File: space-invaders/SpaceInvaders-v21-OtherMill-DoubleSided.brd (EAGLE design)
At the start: 91.4 x 91.4 mm, 26 parts, among them J2-J4 TM4C123GXL, J3-J1 TM4C123GXL, J5 NOKIA_5110, J6 NOKIA_5110, J7 9V, U1 LM7805CT

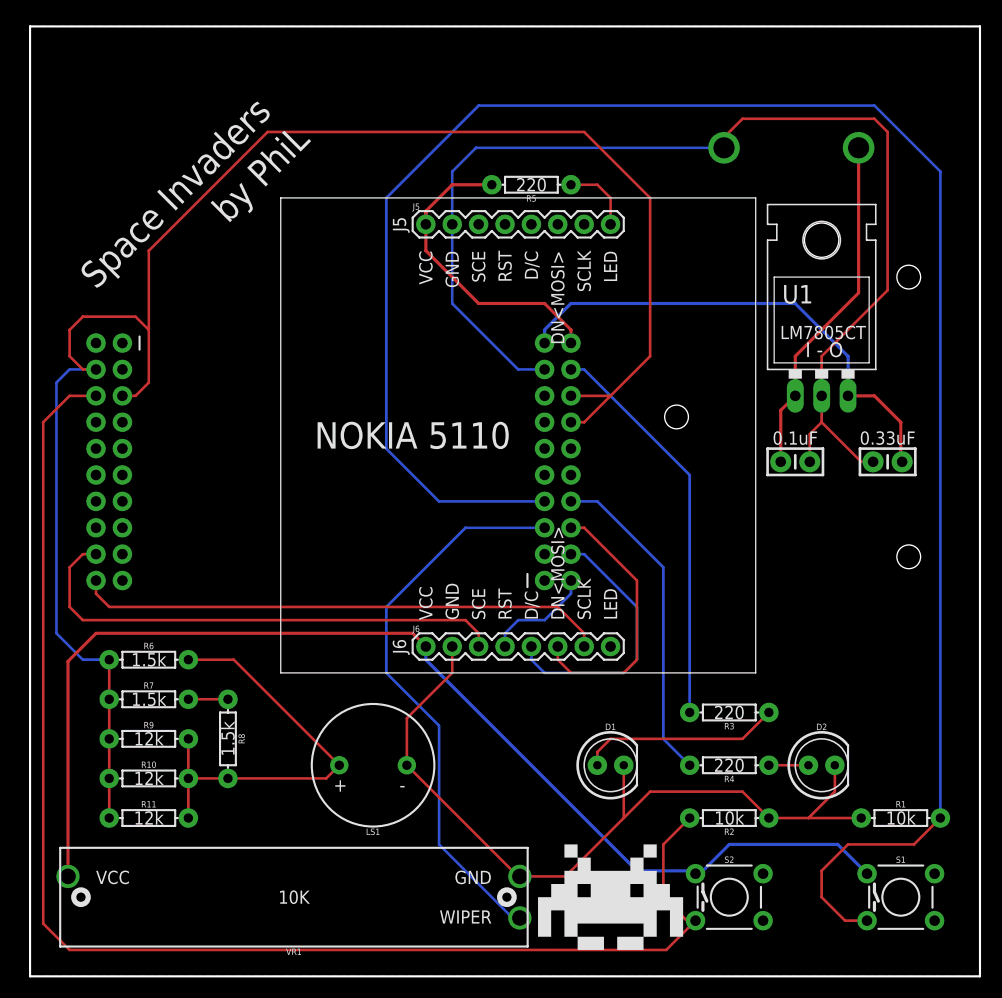
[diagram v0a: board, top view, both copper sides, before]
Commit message: Add versions to file names & Edit stuff
Add versions to file names.
Center Nokia5110 & Edit traces thereof.
Add holes for 9V battery's wires to come through.
v2.1: Replace "SpaceInvaders," "by PhiL," and the sprite icon by Top &
Bottom layers.
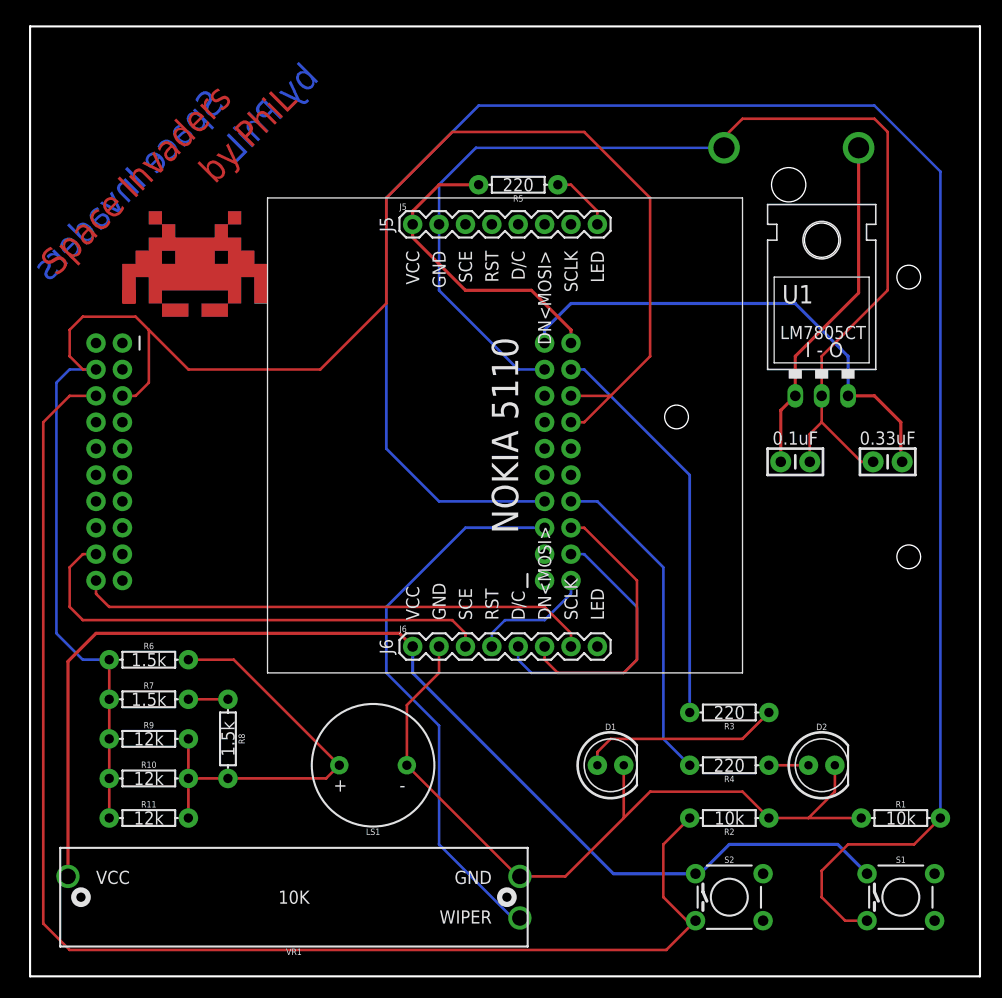
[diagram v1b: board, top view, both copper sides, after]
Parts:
- moved FRAME1 7.62 mm to (12.7, -7.62)
- moved J5 1.27 mm to (36.8, 72.4)
- moved J6 1.27 mm to (36.8, 31.8)
- moved R5 1.27 mm to (47.0, 76.2)
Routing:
- net DAC: track 164.8 -> 169.5 mm
- net PA3: track 48.6 -> 47.3 mm
- net PA2: track 51.1 -> 49.8 mm
- net PA7: track 10.5 -> 11.7 mm
- net PA6: track 26.0 -> 27.3 mm
- net PA5: track 26.0 -> 27.3 mm
- net LED: track 6.88 -> 6.13 mm
- net GND: track 187.8 -> 188.3 mm
- removed copper zone on layer 1, net GND

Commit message: Change the final version to 2.1
v3.0 and v2.1 are the same in structure. The only difference is that one
is supposed to made professionally by a fabrication house and the other
one is made by OtherMill.
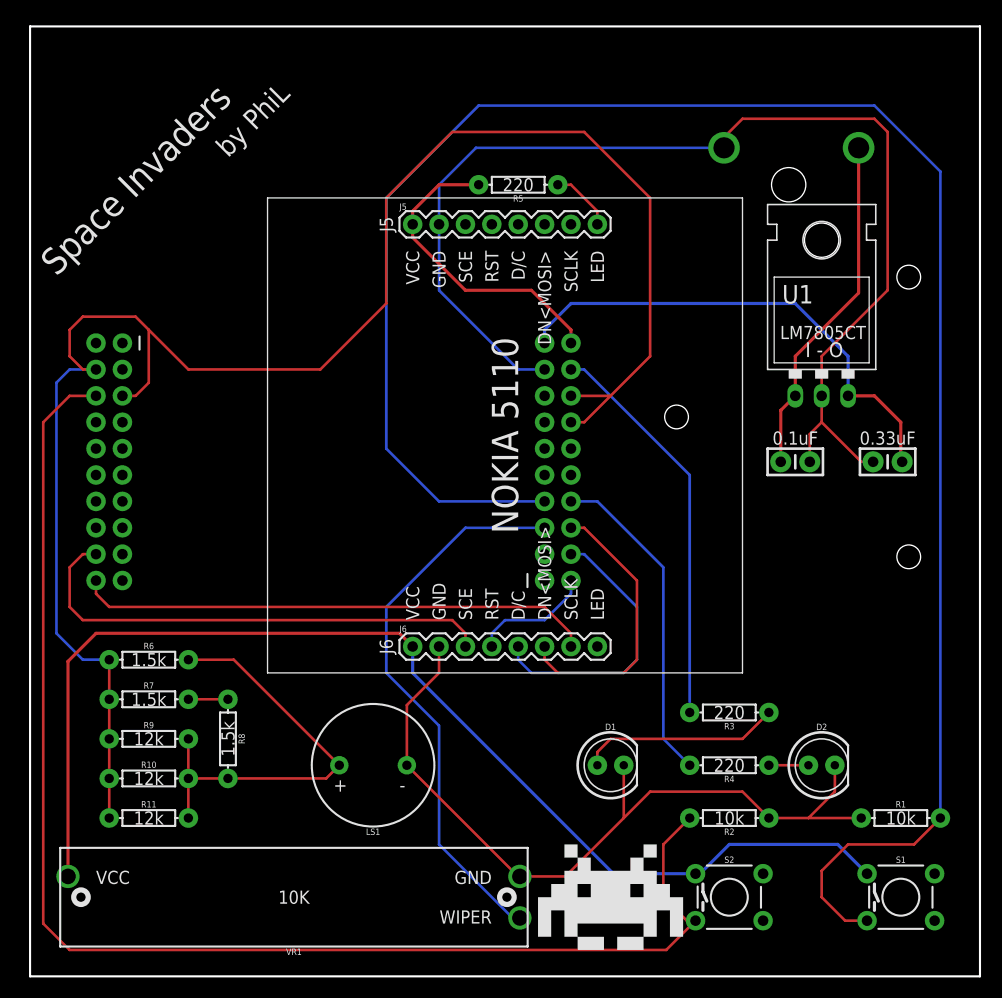
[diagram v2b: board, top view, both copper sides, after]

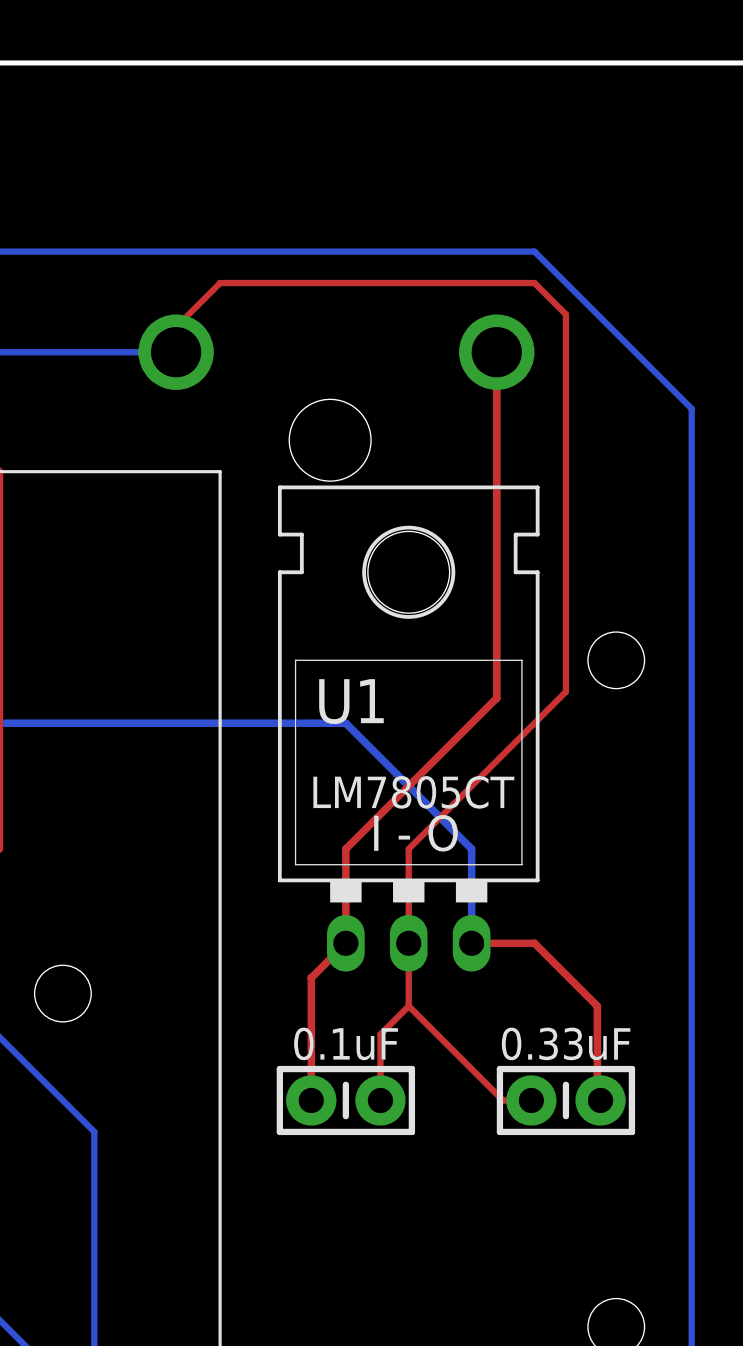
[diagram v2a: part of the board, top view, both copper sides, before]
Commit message: Add SPDT power switch
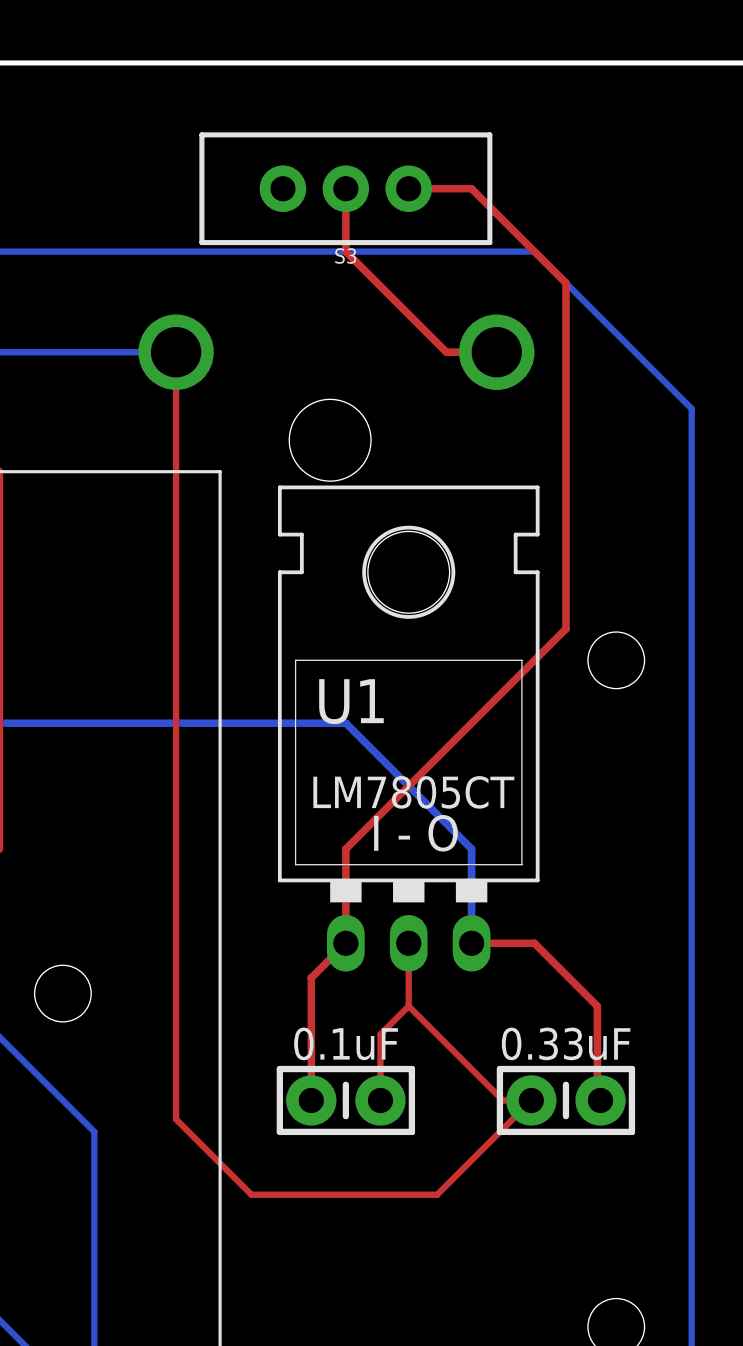
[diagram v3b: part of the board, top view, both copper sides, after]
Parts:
- added S3: POWER_SWITCH, SparkFun-Switches:SWITCH_SPDT_PTH_11.6X4.0MM
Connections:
- new net VIN: J7.V+, S3.2
- net 9V: now also S3.3; no longer J7.V+
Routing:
- net 9V: track 33.3 -> 45.2 mm
- net VIN: track 0.00 -> 10.3 mm
- net GND: track 188.3 -> 190.4 mm
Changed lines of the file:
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@@
 <?xml version="1.0" encoding="utf-8"?>
 <!DOCTYPE eagle SYSTEM "eagle.dtd">
-<eagle version="8.0.1">
+<eagle version="8.0.2">
 <drawing>
 <settings>
@@
 </element>
 <element name="LS1" library="SparkFun-Electromechanical" package="BUZZER-12MM" value="BUZZER" x="33.02" y="20.32" rot="R180">
+<attribute name="PROD_ID" value="COMP-08253" x="33.02" y="20.32" size="1.778" layer="27" rot="R180" display="off"/>
 <attribute name="SF_SKU" value="COM-07950" x="33.02" y="20.32" size="1.778" layer="27" rot="R180" display="off"/>
-<attribute name="PROD_ID" value="COMP-08253" x="33.02" y="20.32" size="1.778" layer="27" rot="R180" display="off"/>
 </element>
 <element name="R1" library="SparkFun-Resistors" package="AXIAL-0.3" value="10k" x="83.82" y="15.24">
@@
 </element>
 <element name="S1" library="SparkFun-Switches" package="TACTILE_SWITCH_PTH_6.0MM" value="SPECIAL" x="83.82" y="7.62">
+<attribute name="PROD_ID" value=" SWCH-08441" x="83.82" y="7.62" size="1.778" layer="27" display="off"/>
 <attribute name="SF_SKU" value="COM-00097" x="83.82" y="7.62" size="1.778" layer="27" display="off"/>
-<attribute name="PROD_ID" value=" SWCH-08441" x="83.82" y="7.62" size="1.778" layer="27" display="off"/>
 </element>
 <element name="S2" library="SparkFun-Switches" package="TACTILE_SWITCH_PTH_6.0MM" value="REGULAR" x="67.31" y="7.62">
+<attribute name="PROD_ID" value=" SWCH-08441" x="67.31" y="7.62" size="1.778" layer="27" display="off"/>
 <attribute name="SF_SKU" value="COM-00097" x="67.31" y="7.62" size="1.778" layer="27" display="off"/>
-<attribute name="PROD_ID" value=" SWCH-08441" x="67.31" y="7.62" size="1.778" layer="27" display="off"/>
 </element>
 <element name="U1" library="SparkFun-IC-Power" package="TO-220-ALT" value="LM7805CT" x="76.2" y="59.69">
+<attribute name="PROD_ID" value="VREG-08450" x="76.2" y="59.69" size="1.778" layer="27" display="off"/>
 <attribute name="SF_ID" value="COM-00107" x="76.2" y="59.69" size="1.778" layer="27" display="off"/>
-<attribute name="PROD_ID" value="VREG-08450" x="76.2" y="59.69" size="1.778" layer="27" display="off"/>
 </element>
 <element name="VR1" library="SparkFun-Resistors" package="SLIDER-MEDIUM" value="10k" x="25.4" y="7.62" rot="R180">
+<attribute name="PROD_ID" value="RES-11931" x="25.4" y="7.62" size="1.778" layer="27" rot="R180" display="off"/>
 <attribute name="SF_SKU" value="COM-11621" x="25.4" y="7.62" size="1.778" layer="27" rot="R180" display="off"/>
-<attribute name="PROD_ID" value="RES-11931" x="25.4" y="7.62" size="1.778" layer="27" rot="R180" display="off"/>
+</element>
+<element name="S3" library="SparkFun-Switches" package="SWITCH_SPDT_PTH_11.6X4.0MM" value="POWER_SWITCH" x="73.66" y="86.36" rot="R90">
+<attribute name="PROD_ID" value="SWCH-08261" x="73.66" y="86.36" size="1.778" layer="27" rot="R90" display="off"/>
+<attribute name="SF_SKU" value="COM-00102" x="73.66" y="86.36" size="1.778" layer="27" rot="R90" display="off"/>
 </element>
 </elements>
@@
 <contactref element="U1" pad="IN"/>
 <contactref element="C2" pad="1"/>
-<contactref element="J7" pad="V+"/>
-<wire x1="79.756" y1="79.756" x2="79.756" y2="65.786" width="0.3048" layer="1"/>
-<wire x1="79.756" y1="65.786" x2="73.66" y2="59.69" width="0.3048" layer="1"/>
-<wire x1="73.66" y1="55.88" x2="73.66" y2="59.69" width="0.3048" layer="1"/>
 <wire x1="72.263" y1="49.53" x2="72.263" y2="54.483" width="0.3048" layer="1"/>
-<wire x1="72.263" y1="54.483" x2="73.66" y2="55.88" width="0.3048" layer="1"/>
+<wire x1="73.66" y1="55.88" x2="72.263" y2="54.483" width="0.3048" layer="1"/>
+<contactref element="S3" pad="3"/>
+<wire x1="76.2" y1="86.36" x2="78.74" y2="86.36" width="0.3048" layer="1"/>
+<wire x1="78.74" y1="86.36" x2="82.55" y2="82.55" width="0.3048" layer="1"/>
+<wire x1="82.55" y1="82.55" x2="82.55" y2="68.58" width="0.3048" layer="1"/>
+<wire x1="82.55" y1="68.58" x2="73.66" y2="59.69" width="0.3048" layer="1"/>
+<wire x1="73.66" y1="59.69" x2="73.66" y2="55.88" width="0.3048" layer="1"/>
 </signal>
 <signal name="GND" airwireshidden="yes">
@@
 <contactref element="R2" pad="P$1"/>
 <contactref element="J5" pad="2"/>
-<wire x1="66.802" y1="79.756" x2="66.802" y2="80.772" width="0.254" layer="1"/>
-<wire x1="66.802" y1="80.772" x2="68.58" y2="82.55" width="0.254" layer="1"/>
-<wire x1="68.58" y1="82.55" x2="81.28" y2="82.55" width="0.254" layer="1"/>
-<wire x1="81.28" y1="82.55" x2="82.55" y2="81.28" width="0.254" layer="1"/>
-<wire x1="82.55" y1="81.28" x2="82.55" y2="66.04" width="0.254" layer="1"/>
-<wire x1="82.55" y1="66.04" x2="76.2" y2="59.69" width="0.254" layer="1"/>
-<wire x1="76.2" y1="55.88" x2="76.2" y2="59.69" width="0.254" layer="1"/>
 <wire x1="81.153" y1="49.53" x2="80.01" y2="49.53" width="0.254" layer="1"/>
 <wire x1="76.2" y1="53.34" x2="80.01" y2="49.53" width="0.254" layer="1"/>
@@
 <wire x1="39.37" y1="29.21" x2="39.37" y2="31.75" width="0.254" layer="1"/>
 <wire x1="36.27" y1="20.32" x2="36.27" y2="26.11" width="0.254" layer="1"/>
-<wire x1="39.37" y1="31.75" x2="46.99" y2="58.42" width="0" layer="19" extent="16-16"/>
+<wire x1="66.802" y1="79.756" x2="66.802" y2="48.768" width="0.254" layer="1"/>
+<wire x1="66.802" y1="48.768" x2="69.85" y2="45.72" width="0.254" layer="1"/>
+<wire x1="69.85" y1="45.72" x2="77.343" y2="45.72" width="0.254" layer="1"/>
+<wire x1="77.343" y1="45.72" x2="81.153" y2="49.53" width="0.254" layer="1"/>
+<wire x1="77.47" y1="20.32" x2="77.343" y2="45.72" width="0" layer="19" extent="1-1"/>
 <wire x1="6.35" y1="60.96" x2="39.37" y2="66.04" width="0" layer="19" extent="16-16"/>
 </signal>
@@
 <wire x1="53.34" y1="58.42" x2="52.07" y2="58.42" width="0.254" layer="16"/>
 </signal>
-<signal name="LED" airwireshidden="yes">
+<signal name="LED">
 <contactref element="R5" pad="P$1"/>
 <contactref element="J5" pad="8"/>
@@
 <wire x1="61.2394" y1="2.54" x2="64.0588" y2="5.3594" width="0.254" layer="1"/>
 </signal>
+<signal name="VIN" class="1">
+<contactref element="J7" pad="V+"/>
+<contactref element="S3" pad="2"/>
+<wire x1="79.756" y1="79.756" x2="77.724" y2="79.756" width="0.3048" layer="1"/>
+<wire x1="77.724" y1="79.756" x2="73.66" y2="83.82" width="0.3048" layer="1"/>
+<wire x1="73.66" y1="83.82" x2="73.66" y2="86.36" width="0.3048" layer="1"/>
+</signal>
 </signals>
